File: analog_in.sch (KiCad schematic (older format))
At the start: 52 parts, among them U3 MCP6004, U4 MCP6004

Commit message: fixed references to old kicad lib
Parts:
- C11, C12, C13, C14, C15, C16, C17, C18, C19, C20: symbol KICAD_Older_Version:C -> Device:C
- R10, R11, R12, R13, R14, R15, R16, R17, R18, R19, R2, R20, R23, R24, R25, R26, R27, R28, R29, R3, R30, R31, R32, R33, R4, R5, R6, R7, R8, R9: symbol KICAD_Older_Version:R -> Device:R
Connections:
- wire segments 206 -> 211

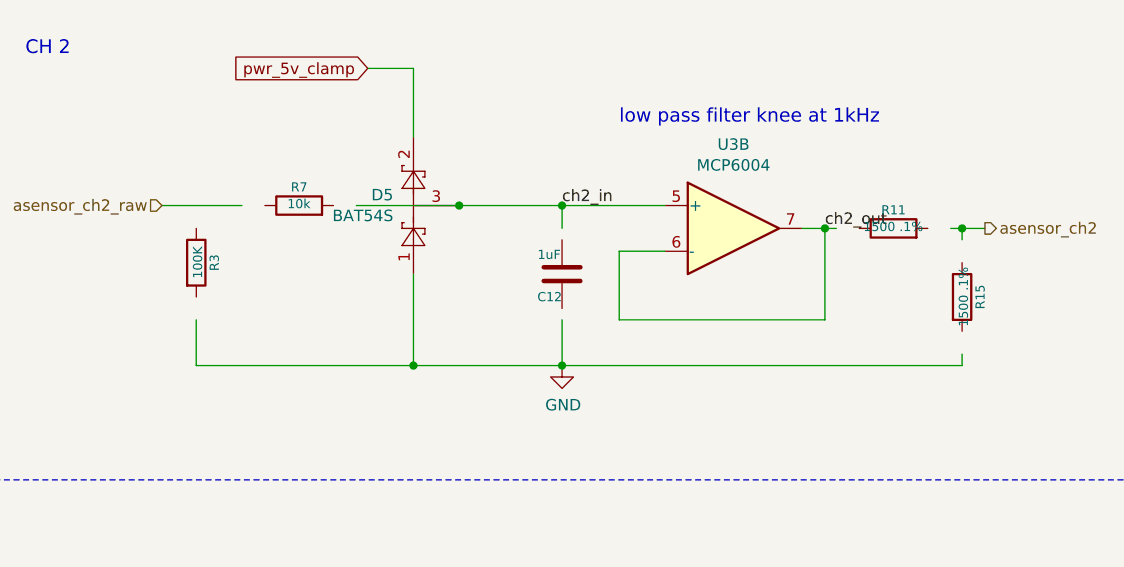
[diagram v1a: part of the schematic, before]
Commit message: migration to kicad 5.1.2
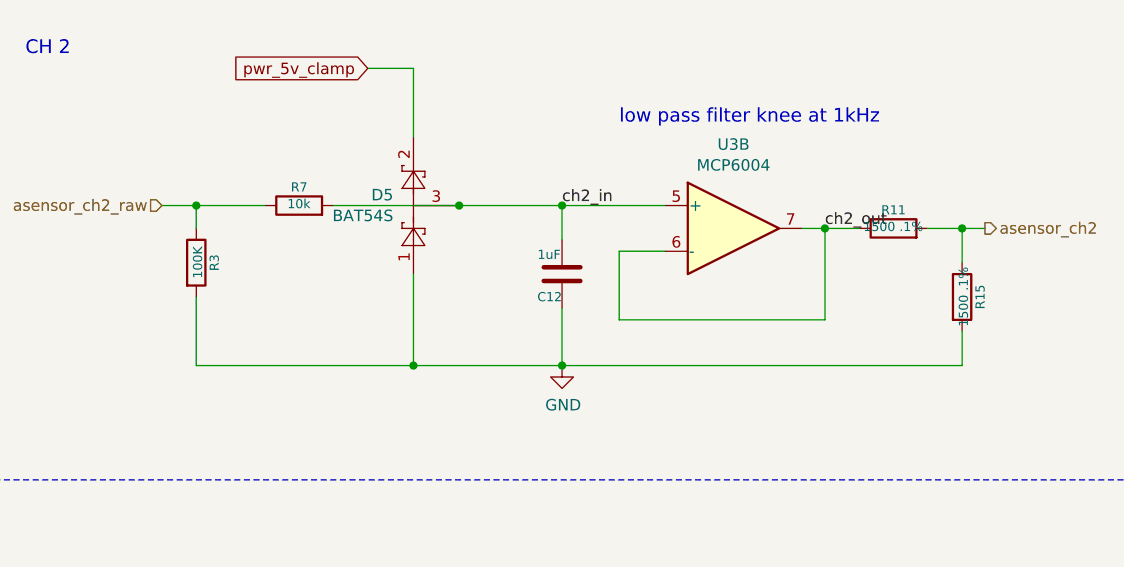
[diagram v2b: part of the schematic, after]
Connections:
- wire segments 211 -> 213
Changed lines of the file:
@@
 EESchema Schematic File Version 4
-LIBS:Tuareg-cache
-EELAYER 26 0
+EELAYER 29 0
 EELAYER END
 $Descr A3 16535 11693
@@
 	3450 4550 3900 4550
 Wire Wire Line
-	5200 4650 5200 4700
-Wire Wire Line
-	5200 5200 5200 5250
-Wire Wire Line
-	1850 5050 1850 5250
-Wire Wire Line
 	1850 5250 2800 5250
 Connection ~ 2800 5250
-Wire Wire Line
-	5150 4650 5200 4650
-Wire Wire Line
-	4650 4650 4600 4650
 Text GLabel 2600 3950 0    50   Input ~ 0
 pwr_5v_clamp
@@
 Wire Wire Line
 	2800 5250 3450 5250
-Wire Wire Line
-	3450 4550 3450 4650
-Wire Wire Line
-	3450 5050 3450 5250
 Connection ~ 3450 5250
 Wire Wire Line
@@
 Wire Notes Line
 	12800 1000 15050 1000
-Wire Wire Line
-	2550 4550 3000 4550
 Wire Wire Line
 	8000 7150 8750 7150
@@
 ch4_out
 Wire Wire Line
-	1700 4550 2050 4550
-Wire Wire Line
 	1700 1950 1850 1950
 Wire Wire Line
@@
 Wire Wire Line
 	13500 1850 13500 2000
+Wire Wire Line
+	1700 4550 1850 4550
+Wire Wire Line
+	2450 4550 3000 4550
+Wire Wire Line
+	1850 4650 1850 4550
+Connection ~ 1850 4550
+Wire Wire Line
+	1850 4550 2150 4550
+Wire Wire Line
+	1850 4950 1850 5250
+Wire Wire Line
+	3450 4550 3450 4700
+Wire Wire Line
+	3450 5000 3450 5250
+Wire Wire Line
+	4600 4650 4750 4650
+Wire Wire Line
+	5050 4650 5200 4650
+Wire Wire Line
+	5200 4650 5200 4800
+Wire Wire Line
+	5200 5100 5200 5250
 $EndSCHEMATC

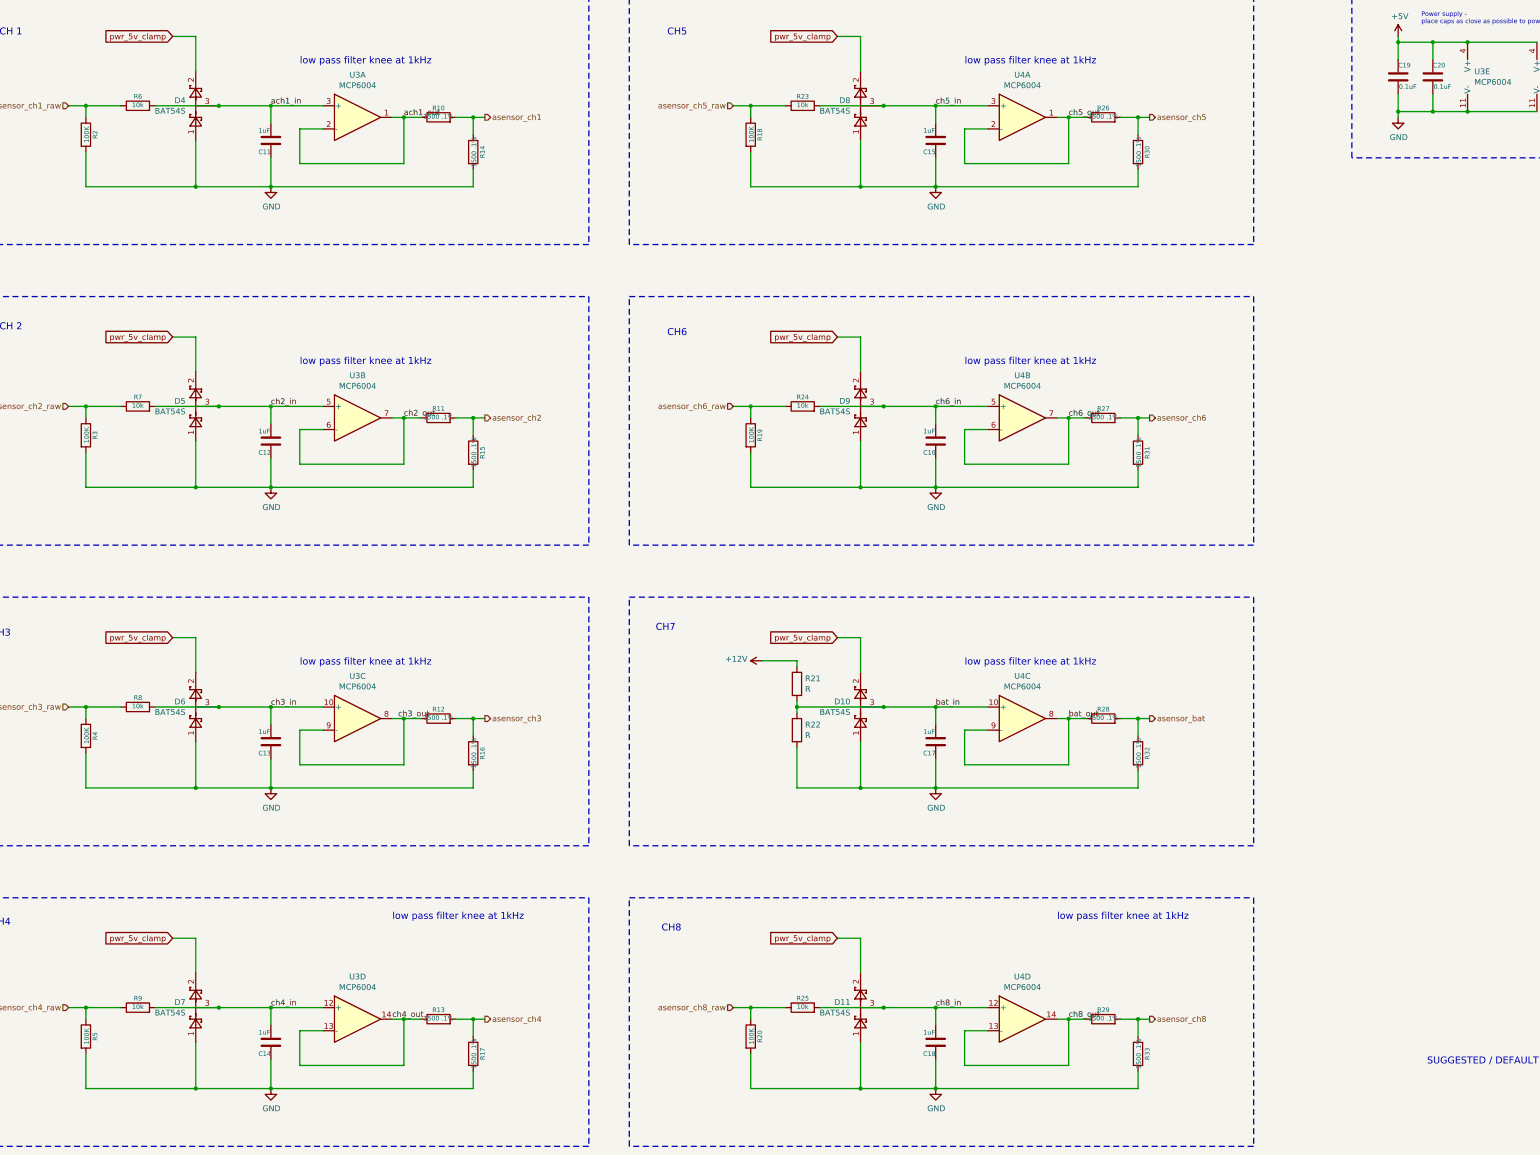
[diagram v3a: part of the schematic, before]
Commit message: added missing component values working on BOM
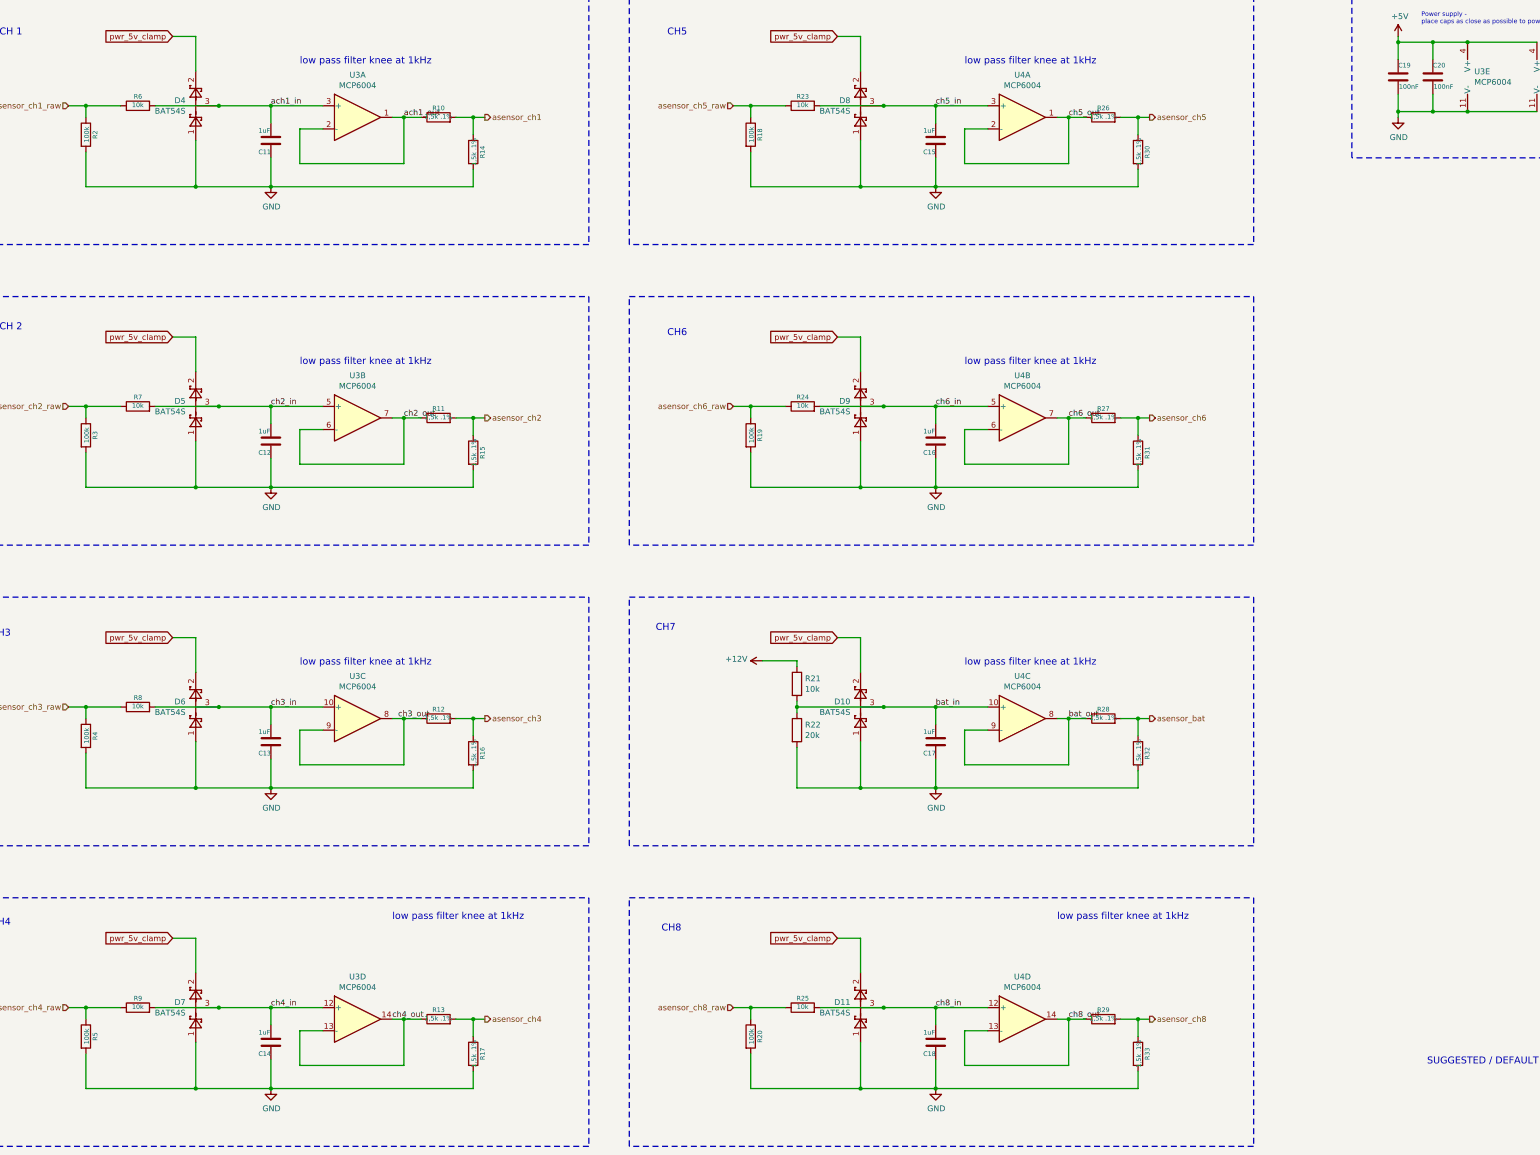
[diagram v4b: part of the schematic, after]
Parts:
- C11, C12, C13, C14, C15, C16, C17, C18: Mouser (none) -> 80-C0805C105M4R
- C19, C20: value 0.1uF -> 100nF; Mouser (none) -> 80-C0805C104Z3V
- D10, D11, D4, D5, D6, D7, D8, D9: Mouser (none) -> 863-BAT54SLT1G
- R10, R11, R12, R13, R14, R15, R16, R17, R26, R27, R28, R29, R30, R31, R32, R33: value 1500 .1% -> 1,5k .1%
- R18, R19, R2, R20, R3, R4, R5: value 100K -> 100k
- R21: value R -> 10k
- R22: value R -> 20k

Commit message: cleaned BOMs
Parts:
- R10, R11, R12, R13, R14, R15, R16, R17, R26, R27, R28, R29, R30, R31, R32, R33: Mouser (none) -> 603-RT0805BRD071K5L
- R18, R19, R2, R20, R3, R4, R5: Mouser (none) -> 279-CRGCQ0805F100K
- R21: Mouser (none) -> 71-CRCW120610K0FKEAC
- R22: Mouser (none) -> 71-CRCW120620K0FKEAC
- R23, R24, R25, R6, R7, R8, R9: Mouser (none) -> 279-CRGCQ0805F10K
- U3, U4: Mouser (none) -> 579-MCP6004T-I/SL
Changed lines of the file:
@@
 F 5 "DIGI,P499KDACT-ND" V 3655 1400 60  0001 C CNN "VEND1,VEND1#"
 F 6 "," H 7175 1425 60  0001 C CNN "VEND2,VEND2#"
+F 7 "279-CRGCQ0805F100K" H 1850 2200 50  0001 C CNN "Mouser"
 	1    1850 2200
 	1    0    0    -1
@@
 F 5 "DIGI,P1.5KDADKR-ND" V 3705 1400 60  0001 C CNN "VEND1,VEND1#"
 F 6 "," H 7225 1425 60  0001 C CNN "VEND2,VEND2#"
+F 7 "603-RT0805BRD071K5L" H 4900 2050 50  0001 C CNN "Mouser"
 	1    4900 2050
 	0    -1   -1   0
@@
 F 5 "DIGI,P1.5KDADKR-ND" V 3505 1700 60  0001 C CNN "VEND1,VEND1#"
 F 6 "," H 7025 1725 60  0001 C CNN "VEND2,VEND2#"
+F 7 "603-RT0805BRD071K5L" H 5200 2350 50  0001 C CNN "Mouser"
 	1    5200 2350
 	1    0    0    -1
@@
 F 5 "DIGI,CR0805-FX-1002ELFCT-ND" V 3655 1400 60  0001 C CNN "VEND1,VEND1#"
 F 6 "," H 7175 1425 60  0001 C CNN "VEND2,VEND2#"
+F 7 "279-CRGCQ0805F10K" H 2300 1950 50  0001 C CNN "Mouser"
 	1    2300 1950
 	0    -1   -1   0
@@
 F 5 "DIGI,P499KDACT-ND" V 3655 4000 60  0001 C CNN "VEND1,VEND1#"
 F 6 "," H 7175 4025 60  0001 C CNN "VEND2,VEND2#"
+F 7 "279-CRGCQ0805F100K" H 1850 4800 50  0001 C CNN "Mouser"
 	1    1850 4800
 	1    0    0    -1
@@
 F 5 "DIGI,P1.5KDADKR-ND" V 3705 4000 60  0001 C CNN "VEND1,VEND1#"
 F 6 "," H 7225 4025 60  0001 C CNN "VEND2,VEND2#"
+F 7 "603-RT0805BRD071K5L" H 4900 4650 50  0001 C CNN "Mouser"
 	1    4900 4650
 	0    -1   -1   0
@@
 F 5 "DIGI,P1.5KDADKR-ND" V 3505 4300 60  0001 C CNN "VEND1,VEND1#"
 F 6 "," H 7025 4325 60  0001 C CNN "VEND2,VEND2#"
+F 7 "603-RT0805BRD071K5L" H 5200 4950 50  0001 C CNN "Mouser"
 	1    5200 4950
 	1    0    0    -1
@@
 F 5 "DIGI,CR0805-FX-1002ELFCT-ND" V 3655 4000 60  0001 C CNN "VEND1,VEND1#"
 F 6 "," H 7175 4025 60  0001 C CNN "VEND2,VEND2#"
+F 7 "279-CRGCQ0805F10K" H 2300 4550 50  0001 C CNN "Mouser"
 	1    2300 4550
 	0    -1   -1   0
@@
 F 5 "DIGI,P499KDACT-ND" V 3655 6600 60  0001 C CNN "VEND1,VEND1#"
 F 6 "," H 7175 6625 60  0001 C CNN "VEND2,VEND2#"
+F 7 "279-CRGCQ0805F100K" H 1850 7400 50  0001 C CNN "Mouser"
 	1    1850 7400
 	1    0    0    -1
@@
 F 5 "DIGI,P1.5KDADKR-ND" V 3705 6600 60  0001 C CNN "VEND1,VEND1#"
 F 6 "," H 7225 6625 60  0001 C CNN "VEND2,VEND2#"
+F 7 "603-RT0805BRD071K5L" H 4900 7250 50  0001 C CNN "Mouser"
 	1    4900 7250
 	0    -1   -1   0
@@
 F 5 "DIGI,P1.5KDADKR-ND" V 3505 6900 60  0001 C CNN "VEND1,VEND1#"
 F 6 "," H 7025 6925 60  0001 C CNN "VEND2,VEND2#"
+F 7 "603-RT0805BRD071K5L" H 5200 7550 50  0001 C CNN "Mouser"
 	1    5200 7550
 	1    0    0    -1
@@
 F 5 "DIGI,CR0805-FX-1002ELFCT-ND" V 3655 6600 60  0001 C CNN "VEND1,VEND1#"
 F 6 "," H 7175 6625 60  0001 C CNN "VEND2,VEND2#"
+F 7 "279-CRGCQ0805F10K" H 2300 7150 50  0001 C CNN "Mouser"
 	1    2300 7150
 	0    -1   -1   0
@@
 F 5 "DIGI,P499KDACT-ND" V 3655 9200 60  0001 C CNN "VEND1,VEND1#"
 F 6 "," H 7175 9225 60  0001 C CNN "VEND2,VEND2#"
+F 7 "279-CRGCQ0805F100K" H 1850 10000 50  0001 C CNN "Mouser"
 	1    1850 10000
 	1    0    0    -1
@@
 F 5 "DIGI,P1.5KDADKR-ND" V 3705 9200 60  0001 C CNN "VEND1,VEND1#"
 F 6 "," H 7225 9225 60  0001 C CNN "VEND2,VEND2#"
+F 7 "603-RT0805BRD071K5L" H 4900 9850 50  0001 C CNN "Mouser"
 	1    4900 9850
 	0    -1   -1   0
@@
 F 5 "DIGI,P1.5KDADKR-ND" V 3505 9500 60  0001 C CNN "VEND1,VEND1#"
 F 6 "," H 7025 9525 60  0001 C CNN "VEND2,VEND2#"
+F 7 "603-RT0805BRD071K5L" H 5200 10150 50  0001 C CNN "Mouser"
 	1    5200 10150
 	1    0    0    -1
@@
 F 5 "DIGI,CR0805-FX-1002ELFCT-ND" V 3655 9200 60  0001 C CNN "VEND1,VEND1#"
 F 6 "," H 7175 9225 60  0001 C CNN "VEND2,VEND2#"
+F 7 "279-CRGCQ0805F10K" H 2300 9750 50  0001 C CNN "Mouser"
 	1    2300 9750
 	0    -1   -1   0
@@
 F 5 "DIGI,P499KDACT-ND" V 9405 1400 60  0001 C CNN "VEND1,VEND1#"
 F 6 "," H 12925 1425 60  0001 C CNN "VEND2,VEND2#"
+F 7 "279-CRGCQ0805F100K" H 7600 2200 50  0001 C CNN "Mouser"
 	1    7600 2200
 	1    0    0    -1
@@
 F 5 "DIGI,P1.5KDADKR-ND" V 9455 1400 60  0001 C CNN "VEND1,VEND1#"
 F 6 "," H 12975 1425 60  0001 C CNN "VEND2,VEND2#"
+F 7 "603-RT0805BRD071K5L" H 10650 2050 50  0001 C CNN "Mouser"
 	1    10650 2050
 	0    -1   -1   0
@@
 F 5 "DIGI,P1.5KDADKR-ND" V 9255 1700 60  0001 C CNN "VEND1,VEND1#"
 F 6 "," H 12775 1725 60  0001 C CNN "VEND2,VEND2#"
+F 7 "603-RT0805BRD071K5L" H 10950 2350 50  0001 C CNN "Mouser"
 	1    10950 2350
 	1    0    0    -1
@@
 F 5 "DIGI,CR0805-FX-1002ELFCT-ND" V 9405 1400 60  0001 C CNN "VEND1,VEND1#"
 F 6 "," H 12925 1425 60  0001 C CNN "VEND2,VEND2#"
+F 7 "279-CRGCQ0805F10K" H 8050 1950 50  0001 C CNN "Mouser"
 	1    8050 1950
 	0    -1   -1   0
@@
 F 5 "DIGI,P499KDACT-ND" V 9405 4000 60  0001 C CNN "VEND1,VEND1#"
 F 6 "," H 12925 4025 60  0001 C CNN "VEND2,VEND2#"
+F 7 "279-CRGCQ0805F100K" H 7600 4800 50  0001 C CNN "Mouser"
 	1    7600 4800
 	1    0    0    -1
@@
 F 5 "DIGI,P1.5KDADKR-ND" V 9455 4000 60  0001 C CNN "VEND1,VEND1#"
 F 6 "," H 12975 4025 60  0001 C CNN "VEND2,VEND2#"
+F 7 "603-RT0805BRD071K5L" H 10650 4650 50  0001 C CNN "Mouser"
 	1    10650 4650
 	0    -1   -1   0
@@
 F 5 "DIGI,P1.5KDADKR-ND" V 9255 4300 60  0001 C CNN "VEND1,VEND1#"
 F 6 "," H 12775 4325 60  0001 C CNN "VEND2,VEND2#"
+F 7 "603-RT0805BRD071K5L" H 10950 4950 50  0001 C CNN "Mouser"
 	1    10950 4950
 	1    0    0    -1
@@
 F 5 "DIGI,CR0805-FX-1002ELFCT-ND" V 9405 4000 60  0001 C CNN "VEND1,VEND1#"
 F 6 "," H 12925 4025 60  0001 C CNN "VEND2,VEND2#"
+F 7 "279-CRGCQ0805F10K" H 8050 4550 50  0001 C CNN "Mouser"
 	1    8050 4550
 	0    -1   -1   0
@@
 F 5 "DIGI,P1.5KDADKR-ND" V 9455 6600 60  0001 C CNN "VEND1,VEND1#"
 F 6 "," H 12975 6625 60  0001 C CNN "VEND2,VEND2#"
+F 7 "603-RT0805BRD071K5L" H 10650 7250 50  0001 C CNN "Mouser"
 	1    10650 7250
 	0    -1   -1   0
@@
 F 5 "DIGI,P1.5KDADKR-ND" V 9255 6900 60  0001 C CNN "VEND1,VEND1#"
 F 6 "," H 12775 6925 60  0001 C CNN "VEND2,VEND2#"
+F 7 "603-RT0805BRD071K5L" H 10950 7550 50  0001 C CNN "Mouser"
 	1    10950 7550
 	1    0    0    -1
@@
 F 5 "DIGI,P499KDACT-ND" V 9405 9200 60  0001 C CNN "VEND1,VEND1#"
 F 6 "," H 12925 9225 60  0001 C CNN "VEND2,VEND2#"
+F 7 "279-CRGCQ0805F100K" H 7600 10000 50  0001 C CNN "Mouser"
 	1    7600 10000
 	1    0    0    -1
@@
 F 5 "DIGI,P1.5KDADKR-ND" V 9455 9200 60  0001 C CNN "VEND1,VEND1#"
 F 6 "," H 12975 9225 60  0001 C CNN "VEND2,VEND2#"
+F 7 "603-RT0805BRD071K5L" H 10650 9850 50  0001 C CNN "Mouser"
 	1    10650 9850
 	0    -1   -1   0
@@
 F 5 "DIGI,P1.5KDADKR-ND" V 9255 9500 60  0001 C CNN "VEND1,VEND1#"
 F 6 "," H 12775 9525 60  0001 C CNN "VEND2,VEND2#"
+F 7 "603-RT0805BRD071K5L" H 10950 10150 50  0001 C CNN "Mouser"
 	1    10950 10150
 	1    0    0    -1
@@
 F 5 "DIGI,CR0805-FX-1002ELFCT-ND" V 9405 9200 60  0001 C CNN "VEND1,VEND1#"
 F 6 "," H 12925 9225 60  0001 C CNN "VEND2,VEND2#"
+F 7 "279-CRGCQ0805F10K" H 8050 9750 50  0001 C CNN "Mouser"
 	1    8050 9750
 	0    -1   -1   0
@@
 F 2 "Resistor_SMD:R_1206_3216Metric" V 7930 6950 50  0001 C CNN
 F 3 "~" H 8000 6950 50  0001 C CNN
+F 4 "71-CRCW120610K0FKEAC " H 8000 6950 50  0001 C CNN "Mouser"
 	1    8000 6950
 	1    0    0    -1
@@
 F 2 "Resistor_SMD:R_1206_3216Metric" V 7930 7350 50  0001 C CNN
 F 3 "~" H 8000 7350 50  0001 C CNN
+F 4 "71-CRCW120620K0FKEAC" H 8000 7350 50  0001 C CNN "Mouser"
 	1    8000 7350
 	1    0    0    -1
@@
 F 2 "boctok_footprints:MCP6004" H 4250 2350 50  0001 C CNN
 F 3 "http://www.ti.com/lit/ds/symlink/lm2902-n.pdf" H 4250 2250 50  0001 C CNN
+F 4 "579-MCP6004T-I/SL" H 4200 2050 50  0001 C CNN "Mouser"
 	1    4200 2050
 	1    0    0    -1
@@
 F 2 "boctok_footprints:MCP6004" H 4250 4950 50  0001 C CNN
 F 3 "http://www.ti.com/lit/ds/symlink/lm2902-n.pdf" H 4250 4850 50  0001 C CNN
+F 4 "579-MCP6004T-I/SL" H 4200 4650 50  0001 C CNN "Mouser"
 	2    4200 4650
 	1    0    0    -1
@@
 F 2 "boctok_footprints:MCP6004" H 4250 7550 50  0001 C CNN
 F 3 "http://www.ti.com/lit/ds/symlink/lm2902-n.pdf" H 4250 7450 50  0001 C CNN
+F 4 "579-MCP6004T-I/SL" H 4200 7250 50  0001 C CNN "Mouser"
 	3    4200 7250
 	1    0    0    -1
@@
 F 2 "boctok_footprints:MCP6004" H 4250 10150 50  0001 C CNN
 F 3 "http://www.ti.com/lit/ds/symlink/lm2902-n.pdf" H 4250 10050 50  0001 C CNN
+F 4 "579-MCP6004T-I/SL" H 4200 9850 50  0001 C CNN "Mouser"
 	4    4200 9850
 	1    0    0    -1
@@
 F 2 "boctok_footprints:MCP6004" H 13950 2000 50  0001 C CNN
 F 3 "http://www.ti.com/lit/ds/symlink/lm2902-n.pdf" H 13950 1900 50  0001 C CNN
+F 4 "579-MCP6004T-I/SL" H 13900 1700 50  0001 C CNN "Mouser"
 	5    13900 1700
 	1    0    0    -1
@@
 F 2 "boctok_footprints:MCP6004" H 10000 2350 50  0001 C CNN
 F 3 "http://www.ti.com/lit/ds/symlink/lm2902-n.pdf" H 10000 2250 50  0001 C CNN
+F 4 "579-MCP6004T-I/SL" H 9950 2050 50  0001 C CNN "Mouser"
 	1    9950 2050
 	1    0    0    -1
@@
 F 2 "boctok_footprints:MCP6004" H 10000 4950 50  0001 C CNN
 F 3 "http://www.ti.com/lit/ds/symlink/lm2902-n.pdf" H 10000 4850 50  0001 C CNN
+F 4 "579-MCP6004T-I/SL" H 9950 4650 50  0001 C CNN "Mouser"
 	2    9950 4650
 	1    0    0    -1
@@
 F 2 "boctok_footprints:MCP6004" H 10000 7550 50  0001 C CNN
 F 3 "http://www.ti.com/lit/ds/symlink/lm2902-n.pdf" H 10000 7450 50  0001 C CNN
+F 4 "579-MCP6004T-I/SL" H 9950 7250 50  0001 C CNN "Mouser"
 	3    9950 7250
 	1    0    0    -1
@@
 F 2 "boctok_footprints:MCP6004" H 10000 10150 50  0001 C CNN
 F 3 "http://www.ti.com/lit/ds/symlink/lm2902-n.pdf" H 10000 10050 50  0001 C CNN
+F 4 "579-MCP6004T-I/SL" H 9950 9850 50  0001 C CNN "Mouser"
 	4    9950 9850
 	1    0    0    -1
@@
 F 2 "boctok_footprints:MCP6004" H 14550 2000 50  0001 C CNN
 F 3 "http://www.ti.com/lit/ds/symlink/lm2902-n.pdf" H 14550 1900 50  0001 C CNN
+F 4 "579-MCP6004T-I/SL" H 14500 1700 50  0001 C CNN "Mouser"
 	5    14500 1700
 	1    0    0    -1
